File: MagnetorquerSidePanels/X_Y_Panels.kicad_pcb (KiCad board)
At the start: 6 copper layers, 82 x 108 mm, 61 parts, among them J6 Through_Hole_1, Q1 BSS138DWQ-7, Q2 MBT2222ADW1T1, Q3 BSS138DWQ-7, Q4 MBT2222ADW1T1, U1 DRV8830DGQ, U2 BD50GC0WEFJ, U3 OPT3001

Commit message: added 3D models to magnetorquer side panel boards
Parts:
- Q1, Q3: value BSS138DWQ-7 -> SOT65P210X110-6N

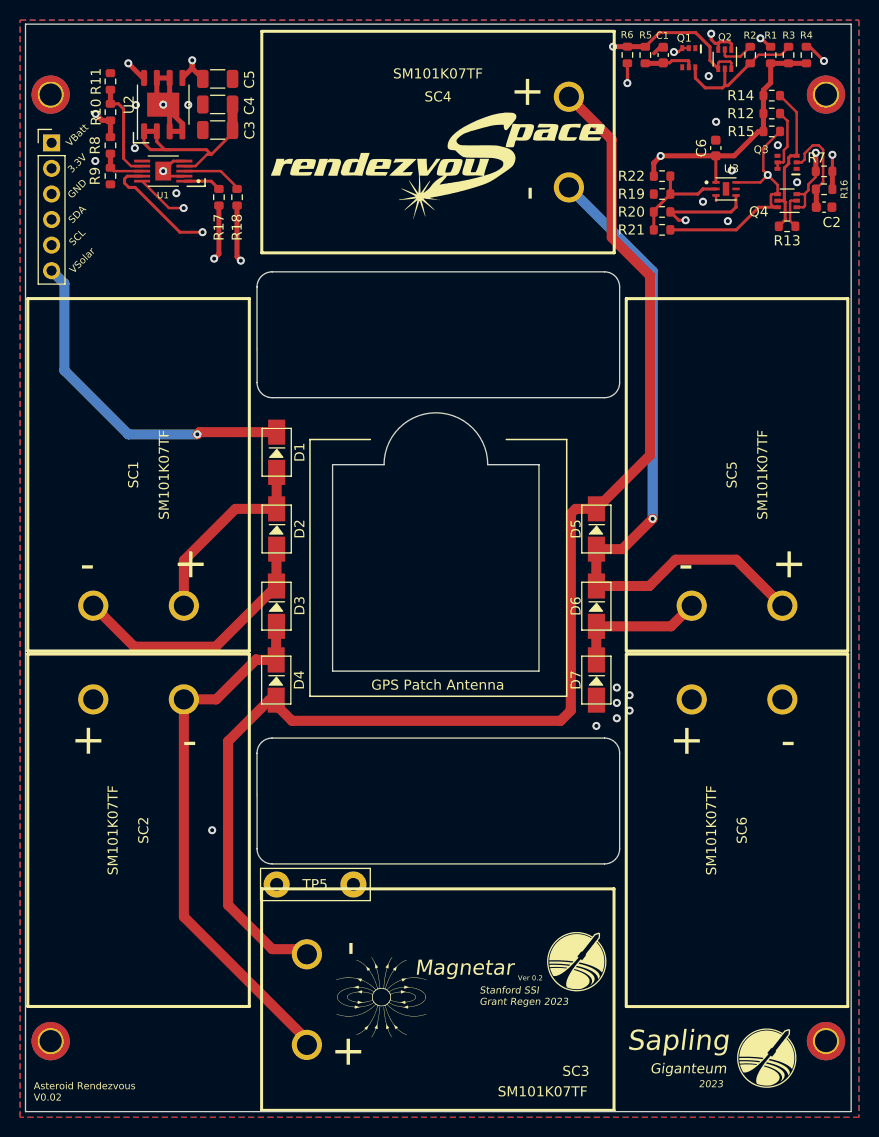
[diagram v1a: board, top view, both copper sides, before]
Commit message: Move hardware from front to back of PCB
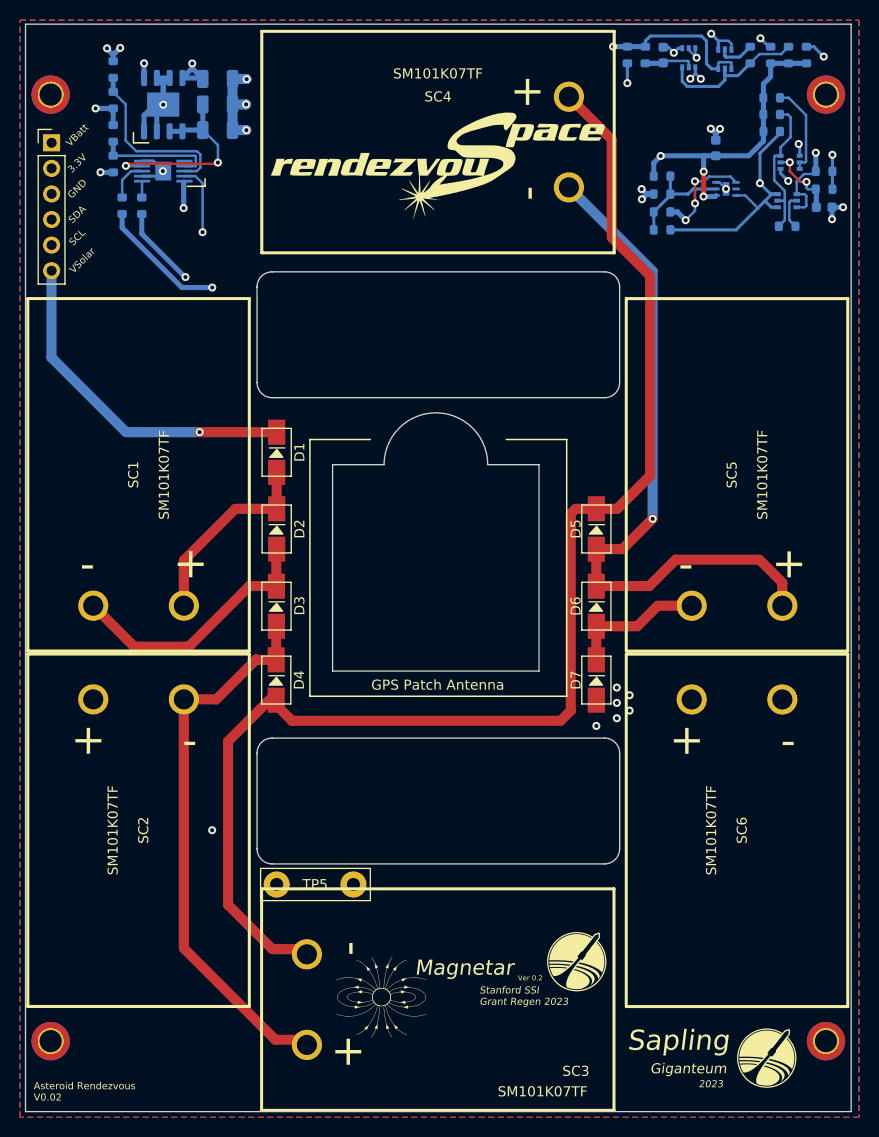
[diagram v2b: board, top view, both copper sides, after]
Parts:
- C1, C2, C3, C4, C5, C6, Q1, Q2, Q3, Q4, R1, R10, R11, R12, R13, R14, R15, R16, R17, R18, R19, R2, R20, R21, R22, R3, R4, R5, R6, R7, R8, R9, U1, U2, U3: moved to B.Cu
- moved R18 11.4 mm to (110.9, 56.0)
- moved R9 10.6 mm to (110.0, 42.5), turned to 90 degrees
- moved R11 8.21 mm to (110.0, 51.9), turned to -90 degrees
- moved R17 7.71 mm to (112.8, 56.0)
- moved R8 4.50 mm to (110.0, 45.5), turned to 90 degrees
- moved R10 2.13 mm to (110.0, 48.8), turned to -90 degrees
- moved R14 1.87 mm to (175.4, 47.0)
- moved R12 1.57 mm to (175.4, 45.3)
- moved Q3 0.30 mm to (177.2, 51.7), turned to 0 degrees
- turned C3 to 180 degrees
- turned C4 to 180 degrees
- turned U1 to 0 degrees
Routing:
- net GND: track 22.5 -> 47.4 mm, vias 20 -> 26
- net Net-(U1-A1): track 4.68 -> 17.8 mm
- net SDA_ISO: track 110.8 -> 104.6 mm
- net Coil_OUT: track 85.4 -> 90.1 mm
- net +3V3: track 89.9 -> 93.2 mm, vias 1 -> 3
- net Net-(Q3A-G2): track 10.1 -> 7.28 mm, vias 0 -> 2
- net Net-(Q3A-D1): track 6.53 -> 9.23 mm
- net Net-(U1-OUT2): track 3.75 -> 1.62 mm
- net Net-(U1-OUT1): track 6.05 -> 4.08 mm
- net Net-(D3-A): track 53.1 -> 54.9 mm
- net Net-(U1-A0): track 10.00 -> 11.7 mm
- net Net-(Q1A-G2): track 12.2 -> 10.8 mm
- net Net-(D5-A): track 68.3 -> 69.6 mm
- net Net-(Q1A-D1): track 14.1 -> 15.4 mm
- net Net-(D4-A): track 132.0 -> 133.2 mm
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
